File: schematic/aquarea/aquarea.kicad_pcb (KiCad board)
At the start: 2 copper layers, 41 x 28 mm, 29 parts, among them J1 RC_CABLE, J2 HP_CABLE, J3 ESP_PROG, Q1 BC847, Q2 BC847, Q3 BC847, Q4 BC847, Q5 BC847, Q6 BC847, Q7 BC847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

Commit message: Update schematic andpcb after tests; add bom and gerbers
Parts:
- removed the D1 at (37.0, 25.5)
- added SW2: Reset, Resistor_SMD:R_0508_1220Metric, B.Cu at (63.5, 27.6)
- Q4: value BC847 -> BC857
- R5: value 10k -> 20k
- moved R6 3.50 mm to (37.0, 39.5)
- moved R7 2.00 mm to (37.0, 42.0)
- moved Q4 0.50 mm to (43.9, 40.5), turned to 0 degrees
- renumbered D3 to D1
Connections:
- C2 pad 1: Net-(D1-A) (its old number) -> +3V3
- Q6 pad 1: Net-(Q4-E) -> Net-(Q4-C)
- R3 pad 1: Net-(U1-~{RST}) -> Net-(R3-Pad1)
- R7 pad 1: Net-(Q4-C) -> Net-(Q4-E)
- U1 pad 7: /ESP_TX -> /ESP_RX
- U2 pad 2: Net-(D1-A) (its old number) -> +3V3
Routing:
- net Net-(R3-Pad1): track 0.00 -> 28.3 mm
- net Net-(U1-~{RST}): track 4.52 -> 27.0 mm
- net Net-(D1-A) (its old number): track 16.3 -> 0.00 mm
- net /ESP_TX: track 37.1 -> 21.9 mm
- net GND: track 32.2 -> 20.9 mm, vias 35 -> 30
- net Net-(Q4-E): track 13.6 -> 4.78 mm
- net /ESP_RTS: track 36.7 -> 28.6 mm
- net /ESP_RX: track 9.38 -> 12.8 mm, vias 0 -> 1
- net /HP_TX: track 74.9 -> 72.5 mm
- net +5V: track 67.4 -> 65.0 mm
- net Net-(Q4-B): track 12.0 -> 14.3 mm
- net Net-(Q3-B): track 13.8 -> 11.9 mm
- net +3V3: track 36.7 -> 38.3 mm
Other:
- board text added: "PRG"
- board text added: "RST"

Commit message: Update schematic
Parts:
- SW2: value Reset -> RESET; footprint Resistor_SMD:R_0508_1220Metric -> Button_Switch_SMD:SW_Push_SPST_NO_Alps_SKRK
- moved SW2 1.68 mm to (64.9, 28.5), turned to 0 degrees
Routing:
- net Net-(SW2-A): track 28.3 -> 25.8 mm
- net Net-(SW2-B): track 27.0 -> 28.6 mm

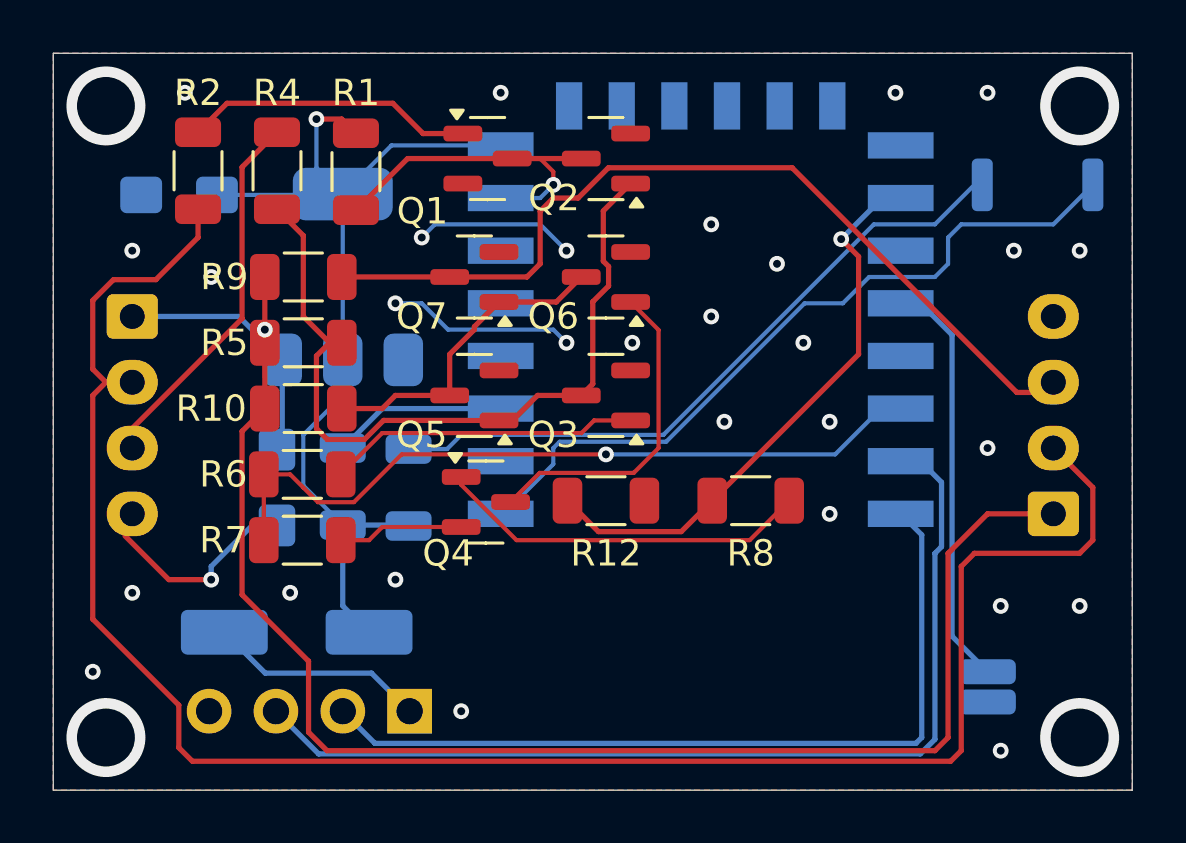
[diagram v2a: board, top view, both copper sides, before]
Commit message: Add proper reset handling and optimize design adround antenna
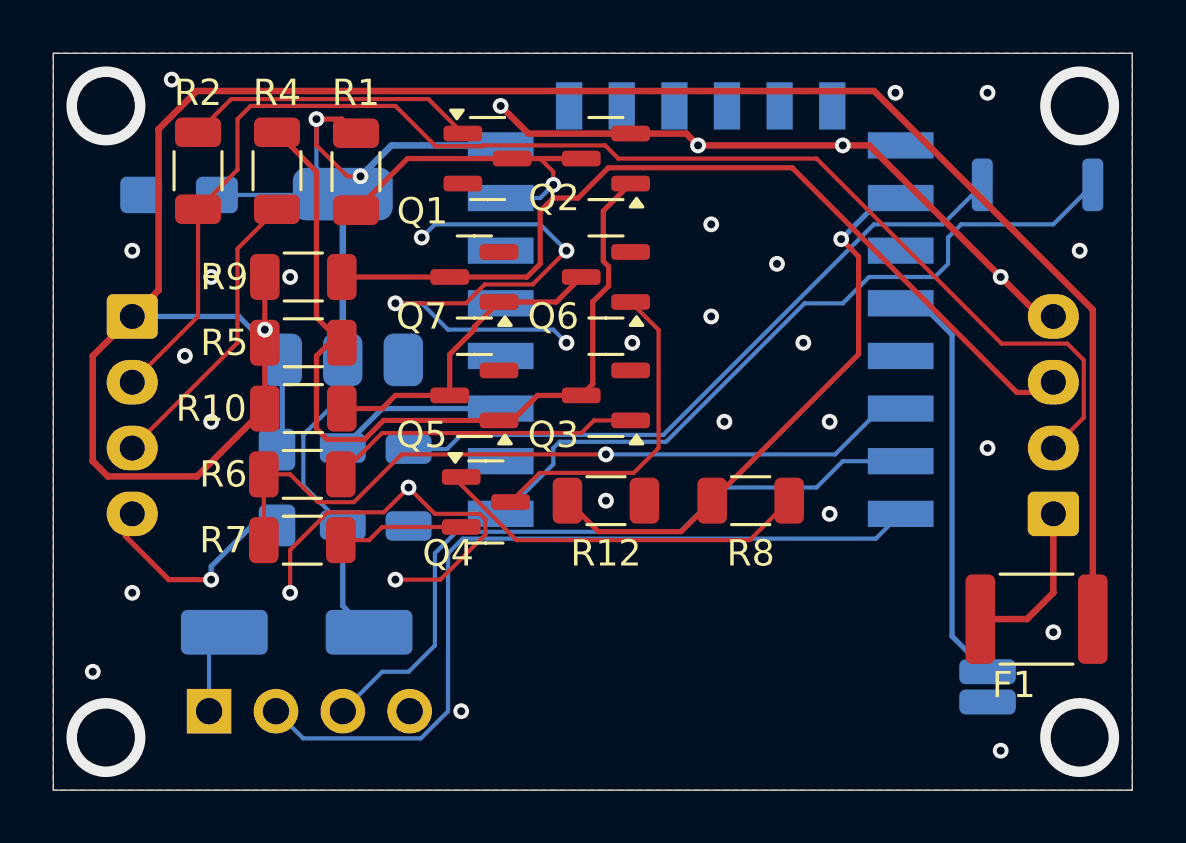
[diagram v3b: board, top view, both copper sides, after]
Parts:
- added F1: 250mA, Fuse:Fuse_1812_4532Metric, F.Cu at (64.9, 45.0)
- moved J3 7.62 mm to (33.4, 48.5), turned to -90 degrees
- turned R3 to 90 degrees
- turned R4 to -90 degrees
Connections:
- J2 pad 1: +5V -> Net-(J2-Pin_1)
- R3 pad 1: Net-(SW2-A) -> GND
- R3 pad 2: +3V3 -> Net-(R3-Pad2)
- SW2 pad 1: Net-(SW2-A) -> Net-(R3-Pad2)
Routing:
- net GND: track 20.9 -> 67.7 mm, vias 30 -> 36
- net Net-(R3-Pad2): track 0.00 -> 26.0 mm
- net Net-(SW2-A): track 25.8 -> 0.00 mm
- net +5V: track 65.0 -> 87.7 mm
- net /HP_TX: track 72.5 -> 51.9 mm
- net /ESP_PRX: track 37.7 -> 27.2 mm
- net Net-(J2-Pin_1): track 0.00 -> 6.19 mm
- net Net-(D1-A): track 8.28 -> 3.24 mm
- net Net-(Q2-B): track 29.8 -> 32.9 mm
- net Net-(J1-Pin_3): track 14.3 -> 11.4 mm
- net +3V3: track 38.3 -> 40.3 mm, vias 1 -> 2
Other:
- board text added: "G RX TX 3V3"
- board text removed: "3V3 TX RX G"
